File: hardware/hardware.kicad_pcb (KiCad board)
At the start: 2 copper layers, 83 x 54.5 mm, 17 parts, among them J1 Screw_Terminal_01x02, J2 Screw_Terminal_01x02, J3 Screw_Terminal_01x02, K1 RM85-2011-35-1005, K2 RM85-2011-35-1005, Q1 BC337, Q2 BC337, U1 XIAO-ESP32-C6

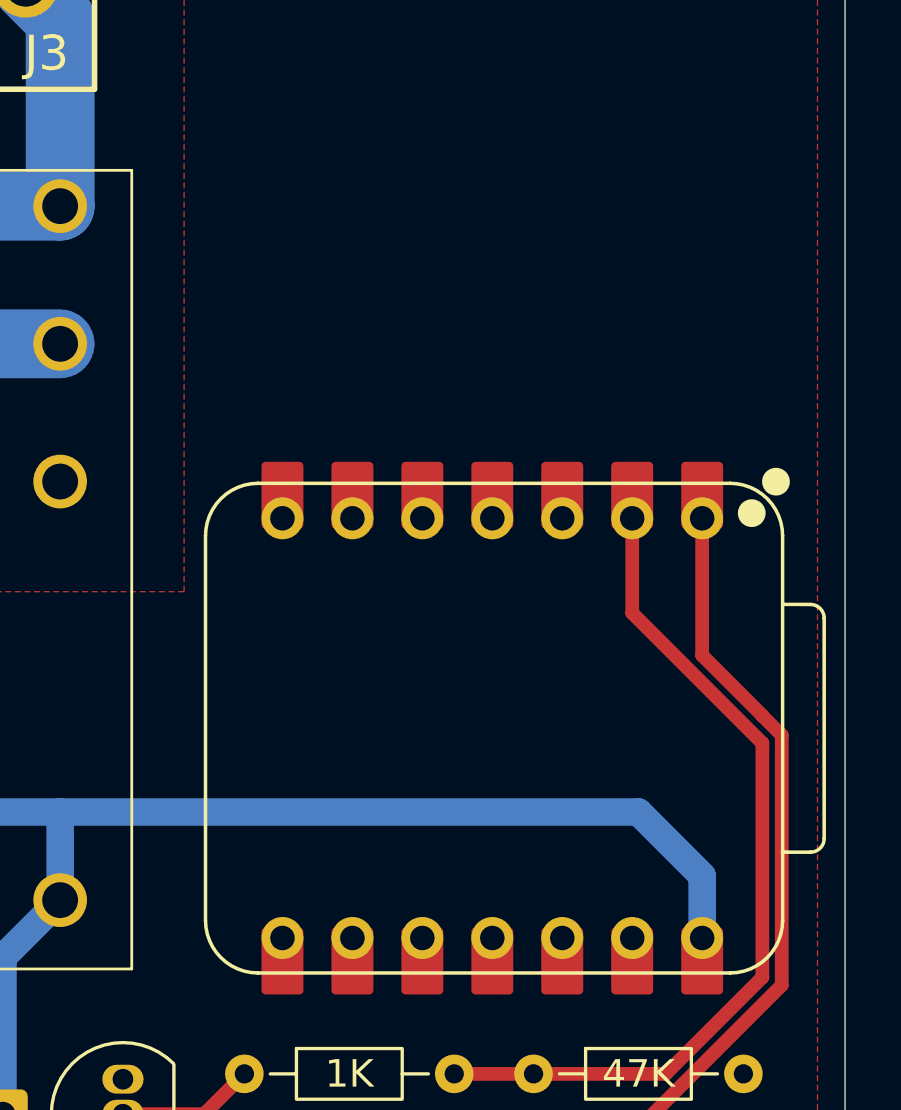
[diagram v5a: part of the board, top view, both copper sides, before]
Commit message: Added headers for extra gpios
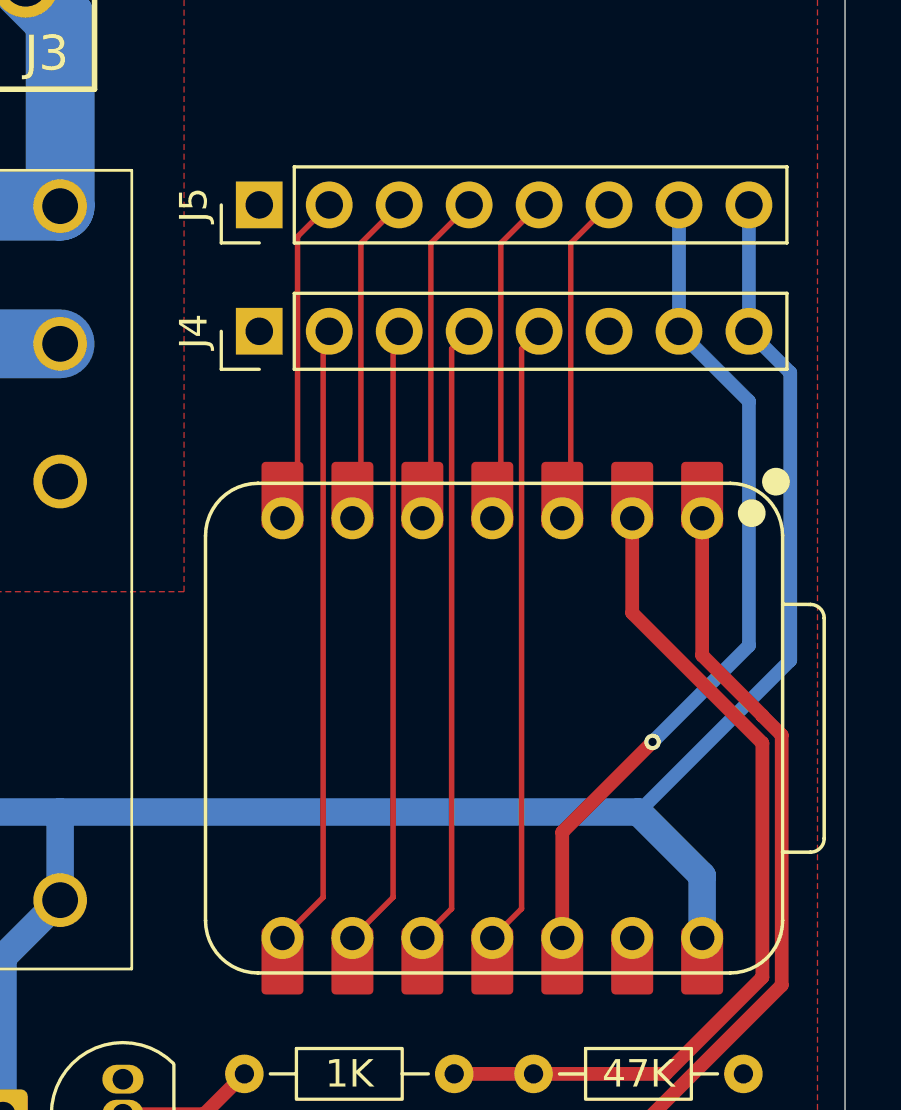
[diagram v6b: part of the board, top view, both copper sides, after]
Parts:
- added J4: Conn_01x08_Pin, Connector_PinHeader_2.54mm:PinHeader_1x08_P2.54mm_Vertical, F.Cu at (92.7, 48.1)
- added J5: Conn_01x08_Pin, Connector_PinHeader_2.54mm:PinHeader_1x08_P2.54mm_Vertical, F.Cu at (92.7, 43.5)
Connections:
- U1 pad 10: unconnected-(U1-GPIO20/D9/MISO-Pad10) -> IO07
- U1 pad 11: unconnected-(U1-GPIO18/D10/MOSI-Pad11) -> IO06
- U1 pad 3: unconnected-(U1-GPIO2/A2/D2-Pad3) -> IO01
- U1 pad 4: unconnected-(U1-GPIO21/D3-Pad4) -> IO02
- U1 pad 5: unconnected-(U1-GPIO22/D4/SDA-Pad5) -> IO03
- U1 pad 6: unconnected-(U1-GPIO23/D5/SCL-Pad6) -> IO04
- U1 pad 7: unconnected-(U1-GPIO16/D6/TX-Pad7) -> IO05
- U1 pad 8: unconnected-(U1-GPIO17/D7/RX-Pad8) -> IO09
- U1 pad 9: unconnected-(U1-GPIO19/D8/SCK-Pad9) -> IO08
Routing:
- net +3V3: track 0.00 -> 30.5 mm, vias 0 -> 1
- net +5V: track 84.1 -> 109.0 mm
- net IO09: track 0.00 -> 22.7 mm
- net IO07: track 0.00 -> 22.7 mm
- net IO08: track 0.00 -> 22.7 mm
- net IO06: track 0.00 -> 22.7 mm
- net IO05: track 0.00 -> 12.1 mm
- net IO03: track 0.00 -> 12.1 mm
- net IO04: track 0.00 -> 12.1 mm
- net IO02: track 0.00 -> 12.1 mm
- net IO01: track 0.00 -> 12.1 mm

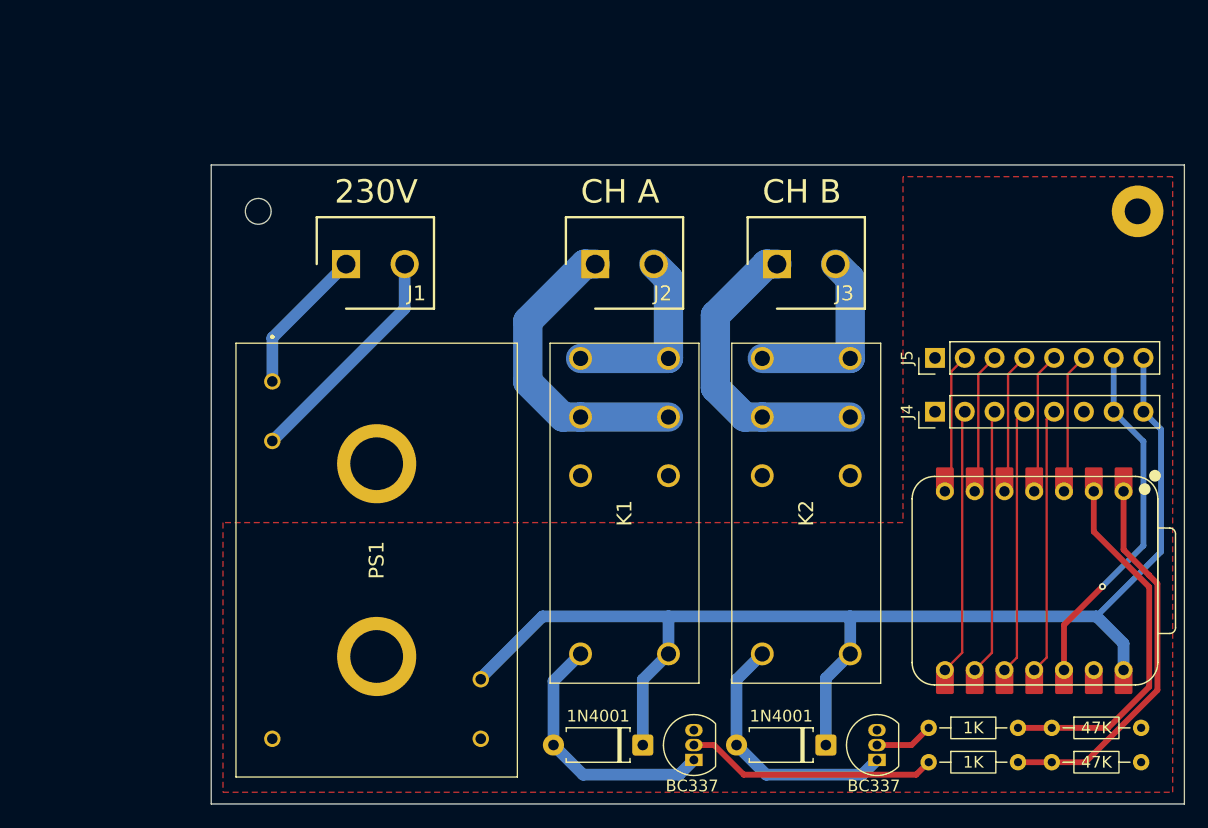
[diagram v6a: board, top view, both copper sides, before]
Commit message: Added status LEDs
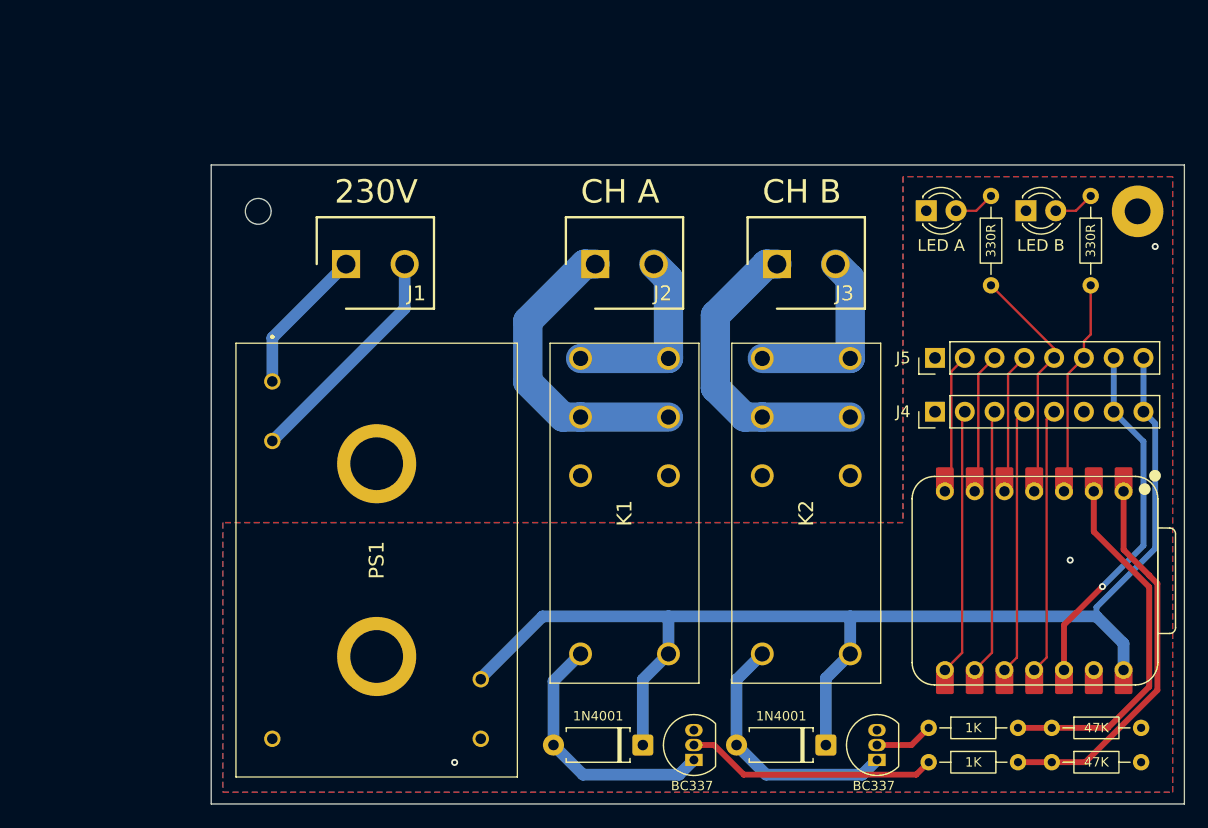
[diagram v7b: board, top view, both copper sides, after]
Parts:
- added D3: LED B, LED_THT:LED_D3.0mm, F.Cu at (100.5, 30.9)
- added D4: LED A, LED_THT:LED_D3.0mm, F.Cu at (92.0, 30.9)
- added R1: 330R, Resistor_THT:R_Axial_DIN0204_L3.6mm_D1.6mm_P7.62mm_Horizontal, F.Cu at (106.0, 29.7)
- added R3: 330R, Resistor_THT:R_Axial_DIN0204_L3.6mm_D1.6mm_P7.62mm_Horizontal, F.Cu at (97.5, 29.7)
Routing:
- net IO02: track 12.1 -> 20.5 mm
- net IO01: track 12.1 -> 18.5 mm
- net Net-(D4-A): track 0.00 -> 3.50 mm
- net Net-(D3-A): track 0.00 -> 3.50 mm
- net GND: vias 0 -> 3
- added copper zone on B.Cu, net GND
